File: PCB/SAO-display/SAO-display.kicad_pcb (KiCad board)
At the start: 2 copper layers, 69.3 x 80 mm, 13 parts, among them CON1 SAO v1.69bis badge, J1 Conn_01x02, J2 Conn_01x02, J3 Conn_01x02, J4 Conn_01x02, J5 Conn_01x02, J6 Conn_01x02, M1 AliExpress 3256806041034057, M1 AliExpress 3256806122258440, M1 AliExpress 3256807183204284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

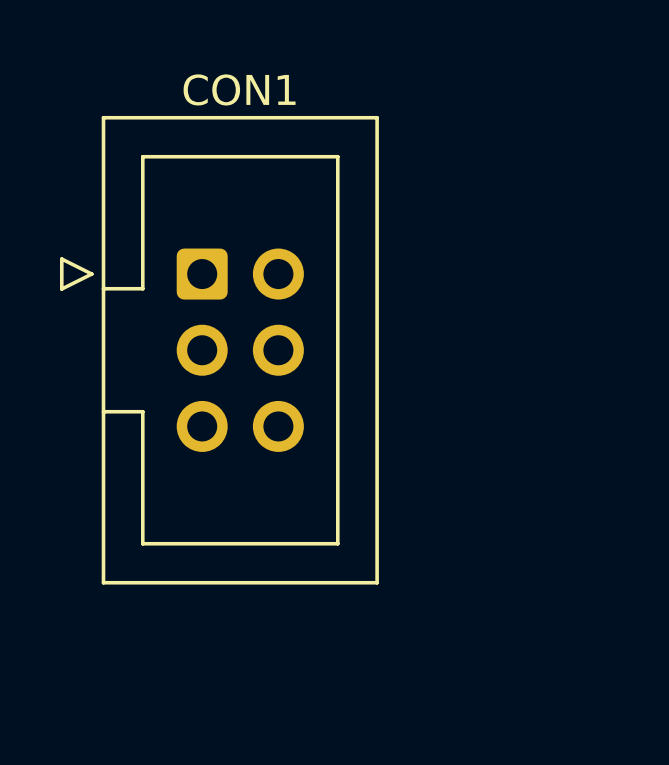
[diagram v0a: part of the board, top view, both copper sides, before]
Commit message: add repo QR code and silk
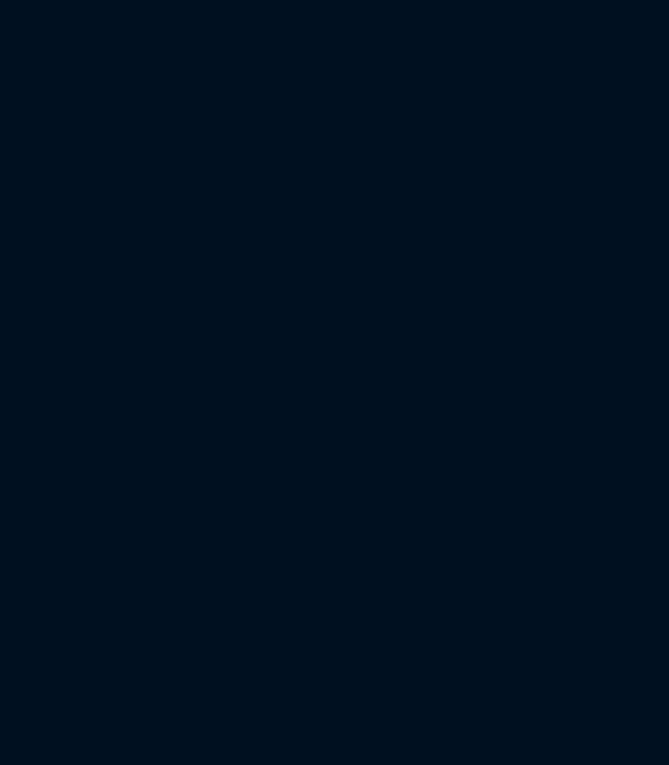
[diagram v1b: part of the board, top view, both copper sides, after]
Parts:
- removed the CON1 at (4.74, 5.62)
- renumbered m1 to M1
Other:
- board text added: "JLCJLCJLCJLC"
- board text added: "github.com/eutectic6337/SAO-display"

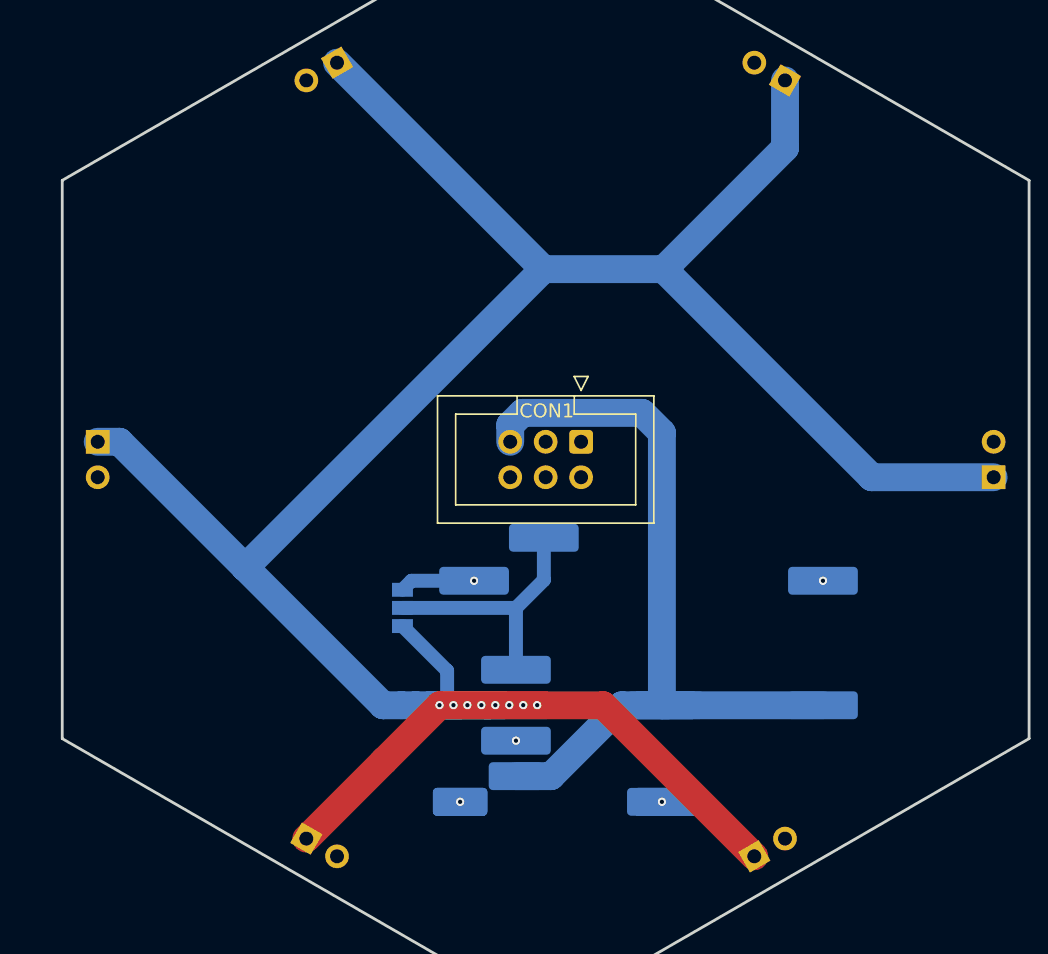
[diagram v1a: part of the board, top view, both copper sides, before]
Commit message: add decoupling capacitors
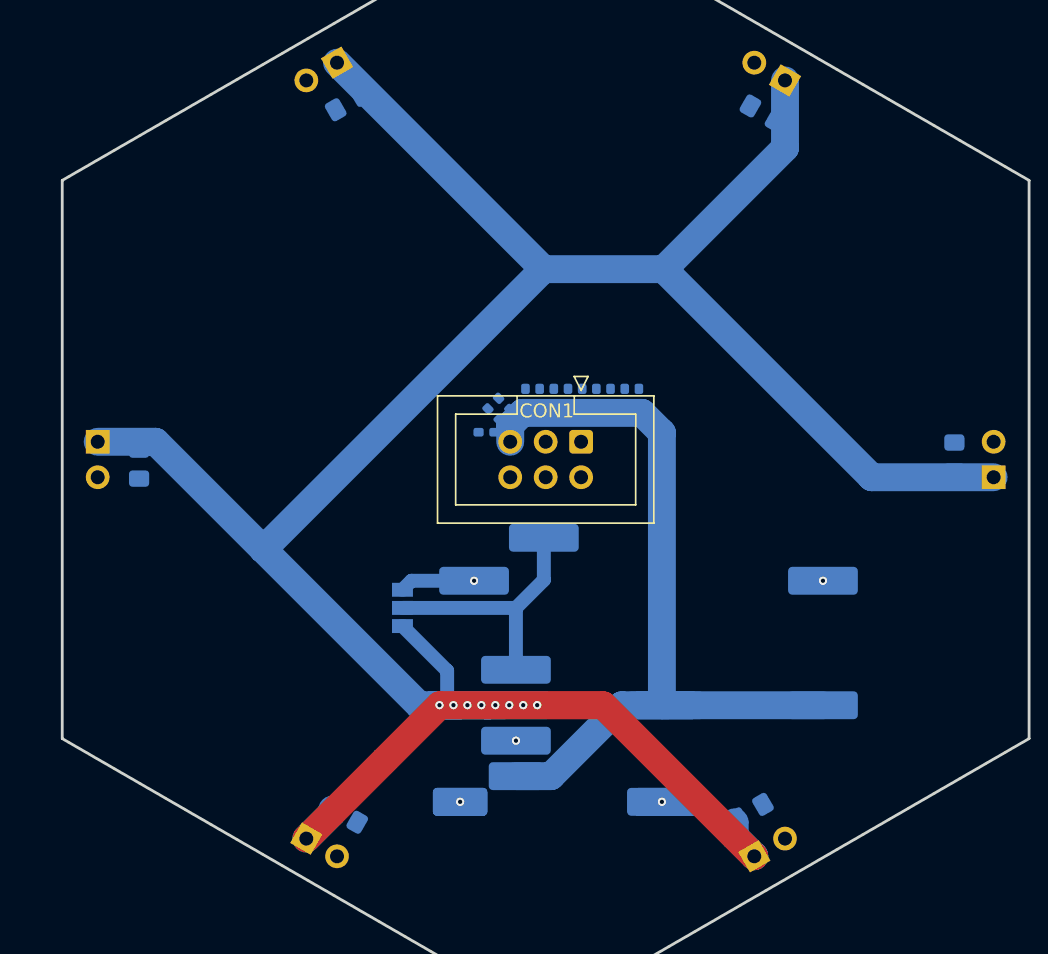
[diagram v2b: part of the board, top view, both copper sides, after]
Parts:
- added C1: 22uF, Capacitor_SMD:C_0805_2012Metric_Pad1.18x1.45mm_HandSolder, B.Cu at (115.6, 75.2)
- added C11: 10uF, Capacitor_SMD:C_0402_1005Metric_Pad0.74x0.62mm_HandSolder, B.Cu at (95.8, 98.0)
- added C12: 10uF, Capacitor_SMD:C_0402_1005Metric_Pad0.74x0.62mm_HandSolder, B.Cu at (96.3, 96.8)
- added C13: 10uF, Capacitor_SMD:C_0402_1005Metric_Pad0.74x0.62mm_HandSolder, B.Cu at (97.0, 96.0)
- added C14: 10uF, Capacitor_SMD:C_0402_1005Metric_Pad0.74x0.62mm_HandSolder, B.Cu at (98.6, 95.5)
- added C15: 10uF, Capacitor_SMD:C_0402_1005Metric_Pad0.74x0.62mm_HandSolder, B.Cu at (99.6, 95.5)
- added C16: 10uF, Capacitor_SMD:C_0402_1005Metric_Pad0.74x0.62mm_HandSolder, B.Cu at (100.6, 95.5)
- added C17: 10uF, Capacitor_SMD:C_0402_1005Metric_Pad0.74x0.62mm_HandSolder, B.Cu at (101.6, 95.5)
- added C18: 10uF, Capacitor_SMD:C_0402_1005Metric_Pad0.74x0.62mm_HandSolder, B.Cu at (102.6, 95.5)
- added C19: 10uF, Capacitor_SMD:C_0402_1005Metric_Pad0.74x0.62mm_HandSolder, B.Cu at (103.6, 95.5)
- added C2: 22uF, Capacitor_SMD:C_0805_2012Metric_Pad1.18x1.45mm_HandSolder, B.Cu at (129.3, 99.8)
- added C20: 10uF, Capacitor_SMD:C_0402_1005Metric_Pad0.74x0.62mm_HandSolder, B.Cu at (104.6, 95.5)
- added C21: 10uF, Capacitor_SMD:C_0402_1005Metric_Pad0.74x0.62mm_HandSolder, B.Cu at (105.7, 95.5)
- added C22: 10uF, Capacitor_SMD:C_0402_1005Metric_Pad0.74x0.62mm_HandSolder, B.Cu at (106.7, 95.5)
- added C3: 22uF, Capacitor_SMD:C_0805_2012Metric_Pad1.18x1.45mm_HandSolder, B.Cu at (114.7, 125.2)
- added C4: 22uF, Capacitor_SMD:C_0805_2012Metric_Pad1.18x1.45mm_HandSolder, B.Cu at (85.6, 125.5)
- added C5: 22uF, Capacitor_SMD:C_0805_2012Metric_Pad1.18x1.45mm_HandSolder, B.Cu at (70.9, 100.3)
- added C6: 22uF, Capacitor_SMD:C_0805_2012Metric_Pad1.18x1.45mm_HandSolder, B.Cu at (85.9, 74.4)
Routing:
- net Vin: track 188.1 -> 192.1 mm

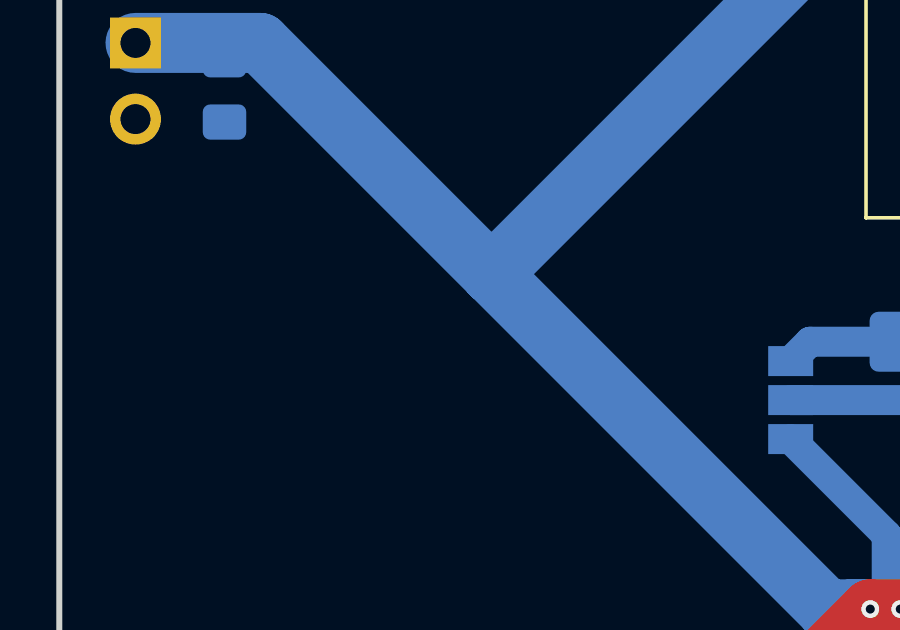
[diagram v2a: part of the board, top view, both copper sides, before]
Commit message: add zener to protect input caps
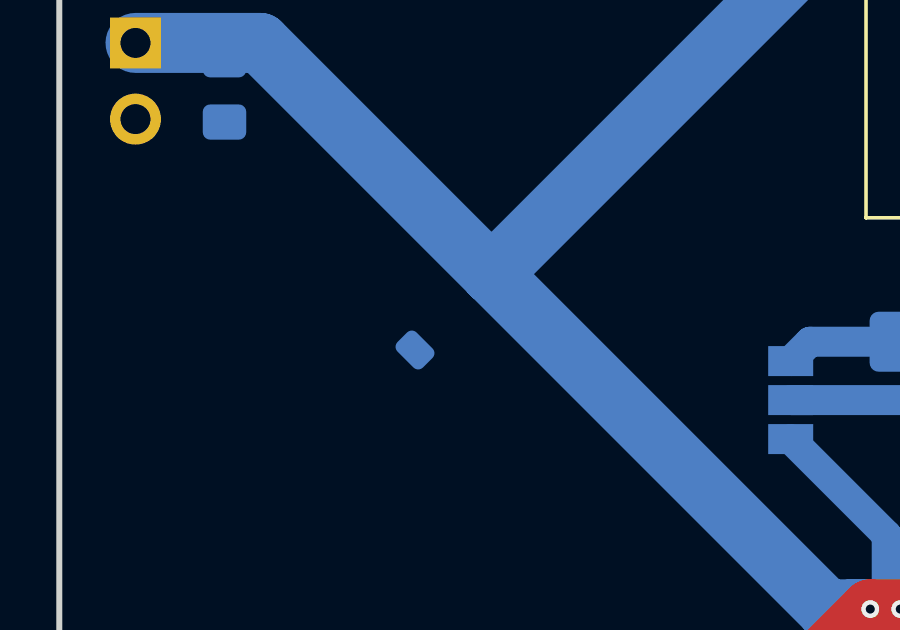
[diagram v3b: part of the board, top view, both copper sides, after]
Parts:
- added D1: 20V, Diode_SMD:D_SOD-123, B.Cu at (78.4, 107.8)

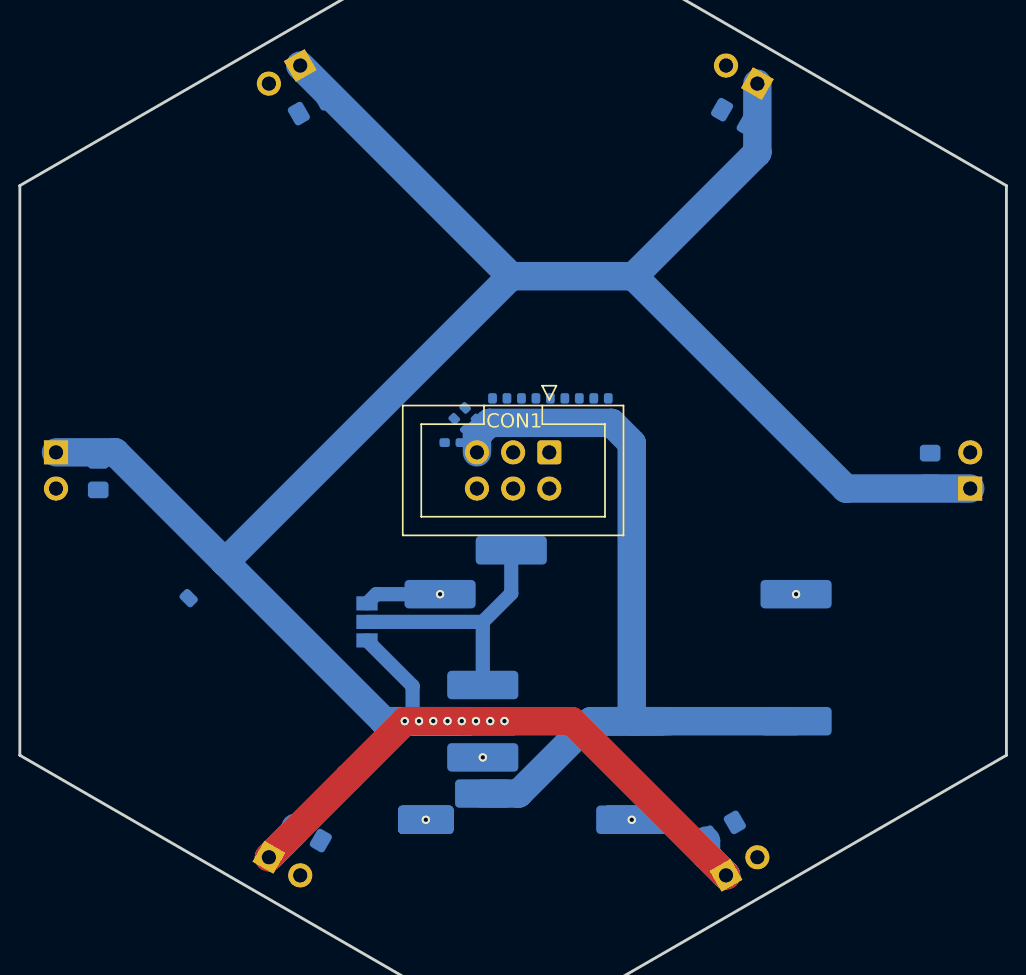
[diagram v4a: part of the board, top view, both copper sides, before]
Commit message: add extra (larger) footprints for alternative capacitors
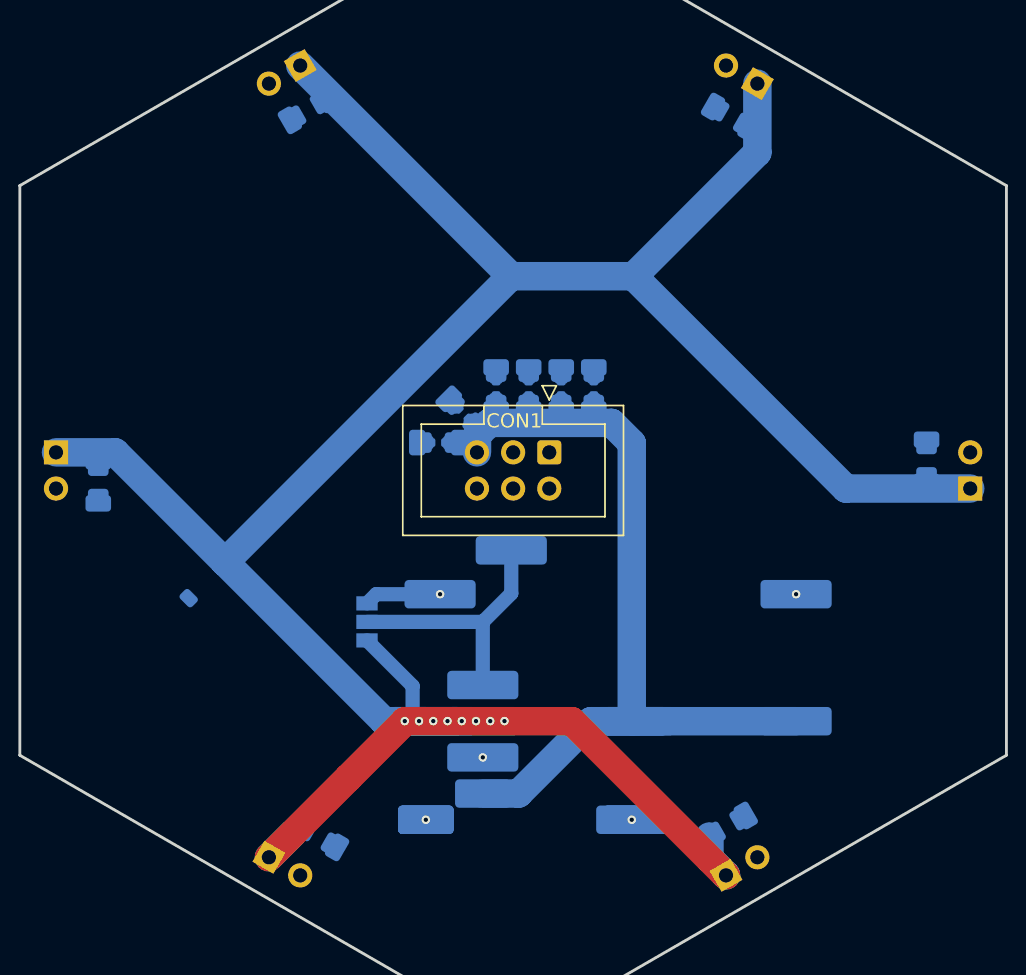
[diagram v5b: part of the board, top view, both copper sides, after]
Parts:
- removed C17, C18, C19, C20, C21, C22: 10uF, Capacitor_SMD:C_0402_1005Metric_Pad0.74x0.62mm_HandSolder
- added C11_0603: C_0603_1608Metric, Capacitor_SMD:C_0603_1608Metric, B.Cu at (96.5, 96.0)
- added C11_0603: C_0603_1608Metric, Capacitor_SMD:C_0603_1608Metric, B.Cu at (101.1, 94.2)
- added C11_0603: C_0603_1608Metric, Capacitor_SMD:C_0603_1608Metric, B.Cu at (98.8, 94.2)
- added C11_0603: C_0603_1608Metric, Capacitor_SMD:C_0603_1608Metric, B.Cu at (105.7, 94.2)
- added C11_0603: C_0603_1608Metric, Capacitor_SMD:C_0603_1608Metric, B.Cu at (103.4, 94.2)
- added C11_0603: C_0603_1608Metric, Capacitor_SMD:C_0603_1608Metric, B.Cu at (94.7, 98.0)
- added C11_0805: C_0805_2012Metric, Capacitor_SMD:C_0805_2012Metric, B.Cu at (105.7, 94.2)
- added C11_0805: C_0805_2012Metric, Capacitor_SMD:C_0805_2012Metric, B.Cu at (98.8, 94.2)
- added C11_0805: C_0805_2012Metric, Capacitor_SMD:C_0805_2012Metric, B.Cu at (101.1, 94.2)
- added C11_0805: C_0805_2012Metric, Capacitor_SMD:C_0805_2012Metric, B.Cu at (94.7, 98.0)
- added C11_0805: C_0805_2012Metric, Capacitor_SMD:C_0805_2012Metric, B.Cu at (96.5, 96.0)
- added C11_0805: C_0805_2012Metric, Capacitor_SMD:C_0805_2012Metric, B.Cu at (103.4, 94.2)
- added C11_1206: C_1206_3216Metric, Capacitor_SMD:C_1206_3216Metric, B.Cu at (105.7, 94.2)
- added C11_1206: C_1206_3216Metric, Capacitor_SMD:C_1206_3216Metric, B.Cu at (98.8, 94.2)
- added C11_1206: C_1206_3216Metric, Capacitor_SMD:C_1206_3216Metric, B.Cu at (103.4, 94.2)
- added C11_1206: C_1206_3216Metric, Capacitor_SMD:C_1206_3216Metric, B.Cu at (96.5, 96.0)
- added C11_1206: C_1206_3216Metric, Capacitor_SMD:C_1206_3216Metric, B.Cu at (101.1, 94.2)
- added C11_1206: C_1206_3216Metric, Capacitor_SMD:C_1206_3216Metric, B.Cu at (94.7, 98.0)
- added C1_1206: C_1206_3216Metric, Capacitor_SMD:C_1206_3216Metric, B.Cu at (129.0, 99.3)
- added C1_1206: C_1206_3216Metric, Capacitor_SMD:C_1206_3216Metric, B.Cu at (115.1, 125.0)
- added C1_1206: C_1206_3216Metric, Capacitor_SMD:C_1206_3216Metric, B.Cu at (85.6, 74.7)
- added C1_1206: C_1206_3216Metric, Capacitor_SMD:C_1206_3216Metric, B.Cu at (86.4, 125.7)
- added C1_1206: C_1206_3216Metric, Capacitor_SMD:C_1206_3216Metric, B.Cu at (70.9, 100.8)
- added C1_1206: C_1206_3216Metric, Capacitor_SMD:C_1206_3216Metric, B.Cu at (115.3, 75.2)
- C1, C2, C3, C4, C5, C6: value 22uF -> 22+uF 50+V
- C11, C12, C13, C14, C15, C16: value 10uF -> 10+uF
- moved C16 5.24 mm to (105.7, 94.2)
- moved C15 4.02 mm to (103.4, 94.2)
- moved C14 2.84 mm to (101.1, 94.2)
- moved C13 2.51 mm to (98.8, 94.2), turned to 90 degrees
- moved C11 1.02 mm to (94.7, 98.0)
- moved C4 0.80 mm to (86.4, 125.7)
- moved C12 0.80 mm to (96.5, 96.0)
- moved C2 0.57 mm to (129.0, 99.3)
- moved C5 0.51 mm to (70.9, 100.8)
- moved C3 0.47 mm to (115.1, 125.0)
- moved C6 0.36 mm to (85.6, 74.7)
- moved C1 0.25 mm to (115.3, 75.2)

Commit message: add another alternative capacitor
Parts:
- C1: value 22+uF 50+V -> 22+uF 25+V

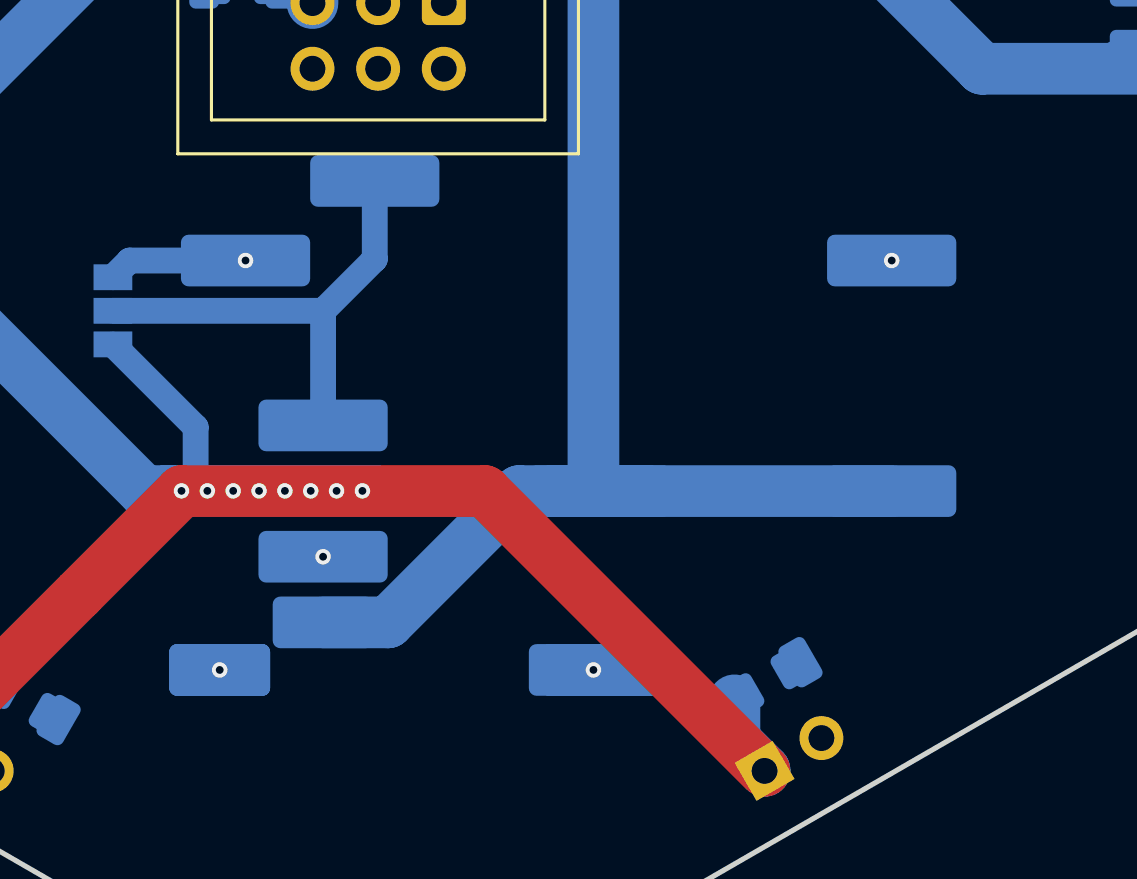
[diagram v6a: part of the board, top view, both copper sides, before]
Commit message: removed selectable-output converter; tweaked footprints
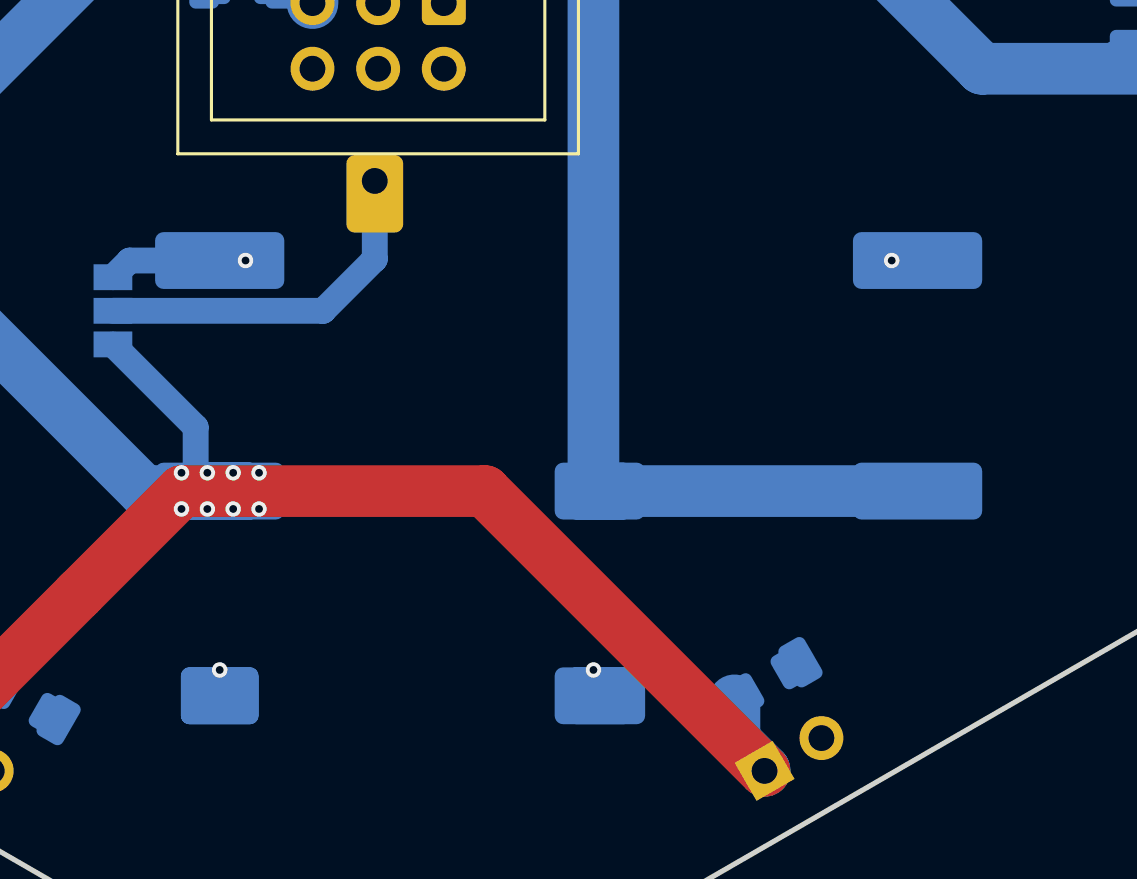
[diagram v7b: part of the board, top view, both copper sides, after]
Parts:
- removed the M1 at (97.9, 117.6)
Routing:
- net Vout: track 57.2 -> 44.1 mm
- net enable: track 18.4 -> 14.0 mm
- net GND: vias 5 -> 4
